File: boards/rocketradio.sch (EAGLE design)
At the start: 29 parts, among them K1 G5LE, T1 2N2222, X1 BU-SMA-H

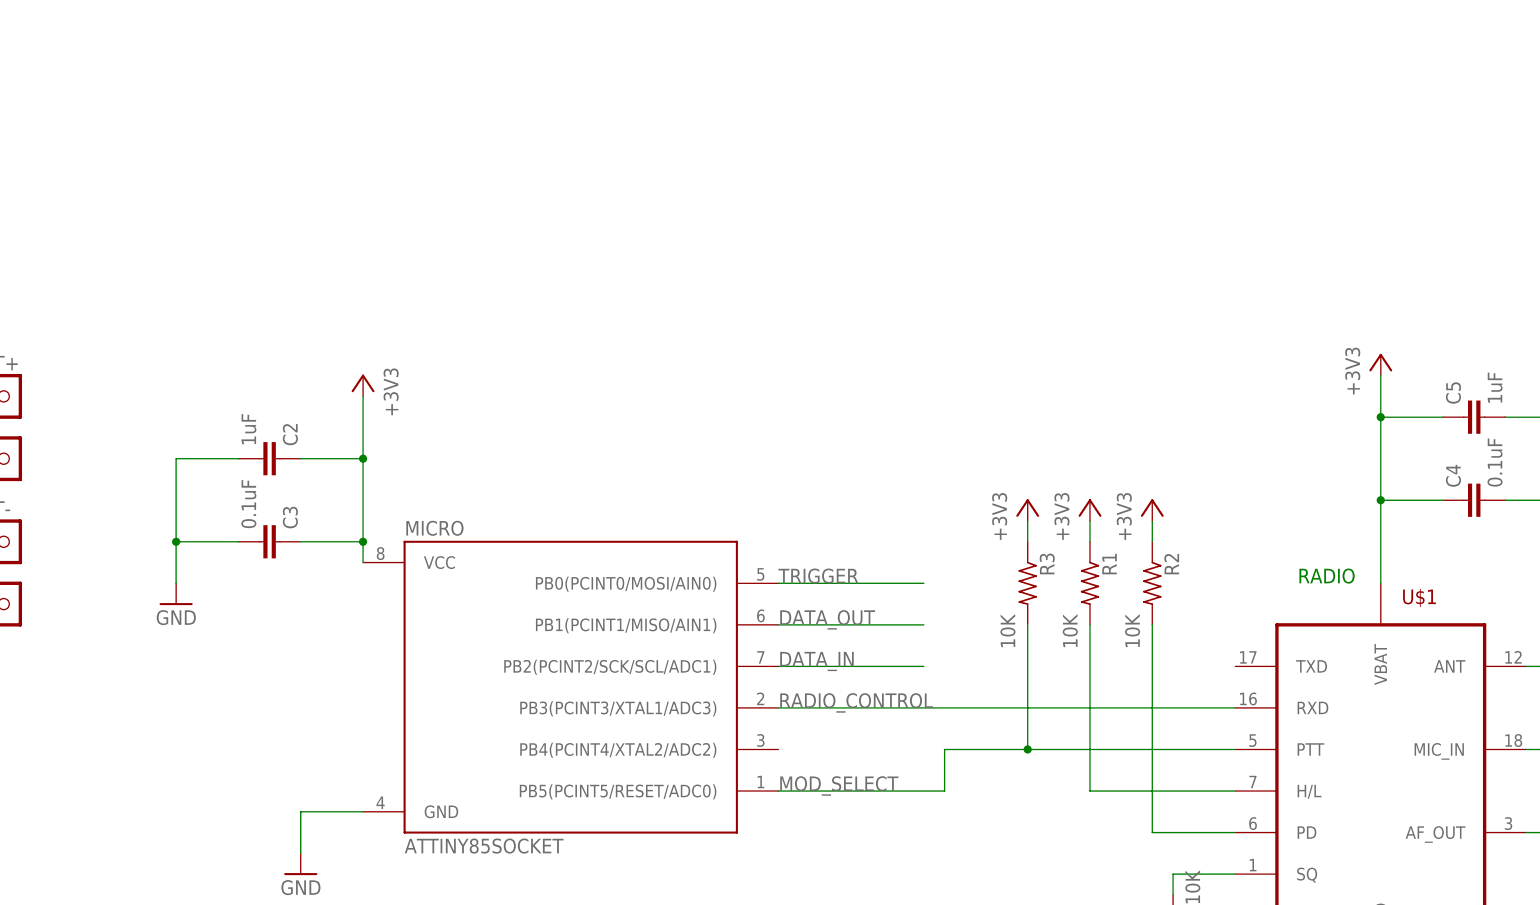
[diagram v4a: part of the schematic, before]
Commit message: use attiny84
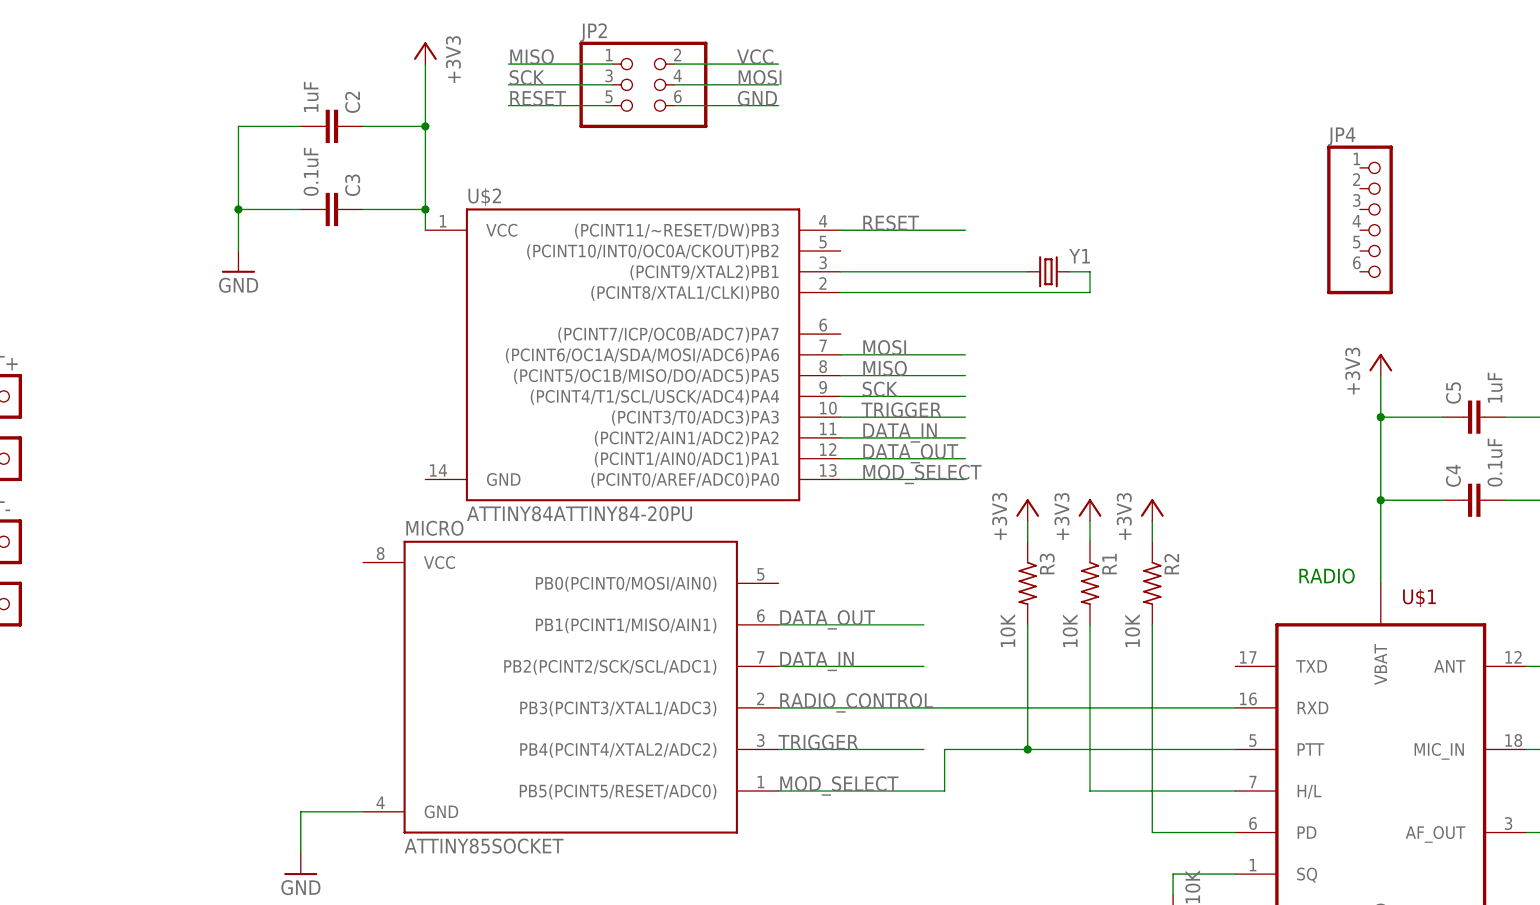
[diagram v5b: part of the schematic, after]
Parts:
- added JP2: (no value), pinhead:PINHD-2X3
- added JP4: (no value), pinhead:PINHD-1X6
- added U$2: ATTINY84ATTINY84-20PU, evan:ATTINY84ATTINY84-20PU
- added Y1: (no value), evan:CRYSTAL
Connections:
- new net MISO: JP2.1, U$2.(PCINT5/OC1B/MISO/DO/ADC5)PA5
- new net MOSI: JP2.4, U$2.(PCINT6/OC1A/SDA/MOSI/ADC6)PA6
- new net N$12: U$2.(PCINT8/XTAL1/CLKI)PB0, Y1.2
- new net N$8: U$2.(PCINT9/XTAL2)PB1, Y1.1
- new net RESET: JP2.5, U$2.(PCINT11/~RESET/DW)PB3
- new net SCK: JP2.3, U$2.(PCINT4/T1/SCL/USCK/ADC4)PA4
- new net VCC: JP2.2
- net +3V3: now also U$2.VCC; no longer MICRO.VCC
- net DATA_IN: now also U$2.(PCINT2/AIN1/ADC2)PA2
- net DATA_OUT: now also U$2.(PCINT1/AIN0/ADC1)PA1
- net GND: now also JP2.6
- net MOD_SELECT: now also U$2.(PCINT0/AREF/ADC0)PA0
- net TRIGGER: now also MICRO.PB4(PCINT4/XTAL2/ADC2), U$2.(PCINT3/T0/ADC3)PA3; no longer MICRO.PB0(PCINT0/MOSI/AIN0)
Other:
- moved on the sheet: C2, C3
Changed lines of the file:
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@@
 <part name="NC" library="evan" deviceset="PINHD-1X1" device=""/>
 <part name="NO" library="evan" deviceset="PINHD-1X1" device=""/>
+<part name="U$2" library="evan" deviceset="ATTINY84" device="ATTINY84-20PU"/>
+<part name="JP2" library="pinhead" deviceset="PINHD-2X3" device=""/>
+<part name="Y1" library="evan" deviceset="CRYSTAL" device=""/>
+<part name="JP4" library="pinhead" deviceset="PINHD-1X6" device=""/>
 </parts>
 <sheets>
@@
 <instance part="GND6" gate="1" x="-144.78" y="25.4" rot="MR0"/>
 <instance part="MICRO" gate="G$1" x="-96.52" y="88.9"/>
-<instance part="+3V4" gate="G$1" x="-121.92" y="127" rot="MR0"/>
-<instance part="C2" gate="G$1" x="-132.08" y="116.84" rot="MR90"/>
-<instance part="C3" gate="G$1" x="-132.08" y="106.68" rot="MR90"/>
-<instance part="GND8" gate="1" x="-144.78" y="99.06" rot="MR0"/>
+<instance part="+3V4" gate="G$1" x="-114.3" y="167.64" rot="MR0"/>
+<instance part="C2" gate="G$1" x="-124.46" y="157.48" rot="MR90"/>
+<instance part="C3" gate="G$1" x="-124.46" y="147.32" rot="MR90"/>
+<instance part="GND8" gate="1" x="-137.16" y="139.7" rot="MR0"/>
 <instance part="GND9" gate="1" x="-129.54" y="66.04" rot="MR0"/>
 <instance part="GND10" gate="1" x="-129.54" y="-7.62" rot="MR0"/>
@@
 <instance part="NC" gate="G$1" x="88.9" y="33.02"/>
 <instance part="NO" gate="G$1" x="53.34" y="33.02" rot="R180"/>
+<instance part="U$2" gate="G$1" x="-88.9" y="129.54"/>
+<instance part="JP2" gate="A" x="-88.9" y="162.56"/>
+<instance part="Y1" gate="G$1" x="-38.1" y="139.7"/>
+<instance part="JP4" gate="A" x="2.54" y="144.78"/>
 </instances>
 <busses>
@@
 <segment>
 <pinref part="C3" gate="G$1" pin="2"/>
-<wire x1="-137.16" y1="106.68" x2="-144.78" y2="106.68" width="0.1524" layer="91"/>
-<wire x1="-144.78" y1="106.68" x2="-144.78" y2="101.6" width="0.1524" layer="91"/>
+<wire x1="-129.54" y1="147.32" x2="-137.16" y2="147.32" width="0.1524" layer="91"/>
+<wire x1="-137.16" y1="147.32" x2="-137.16" y2="142.24" width="0.1524" layer="91"/>
 <pinref part="C2" gate="G$1" pin="2"/>
-<wire x1="-144.78" y1="106.68" x2="-144.78" y2="116.84" width="0.1524" layer="91"/>
-<wire x1="-144.78" y1="116.84" x2="-137.16" y2="116.84" width="0.1524" layer="91"/>
-<junction x="-144.78" y="106.68"/>
+<wire x1="-137.16" y1="147.32" x2="-137.16" y2="157.48" width="0.1524" layer="91"/>
+<wire x1="-137.16" y1="157.48" x2="-129.54" y2="157.48" width="0.1524" layer="91"/>
+<junction x="-137.16" y="147.32"/>
 <pinref part="GND8" gate="1" pin="GND"/>
 </segment>
@@
 <wire x1="40.64" y1="7.62" x2="40.64" y2="10.16" width="0.1524" layer="91"/>
 </segment>
+<segment>
+<pinref part="JP2" gate="A" pin="6"/>
+<wire x1="-83.82" y1="160.02" x2="-71.12" y2="160.02" width="0.1524" layer="91"/>
+<label x="-76.2" y="160.02" size="1.778" layer="95"/>
+</segment>
 </net>
 <net name="+3V3" class="0">
@@
 <pinref part="+3V4" gate="G$1" pin="+3V3"/>
 <pinref part="C2" gate="G$1" pin="1"/>
-<wire x1="-121.92" y1="106.68" x2="-121.92" y2="116.84" width="0.1524" layer="91"/>
-<wire x1="-121.92" y1="116.84" x2="-121.92" y2="124.46" width="0.1524" layer="91"/>
-<wire x1="-129.54" y1="116.84" x2="-121.92" y2="116.84" width="0.1524" layer="91"/>
-<junction x="-121.92" y="116.84"/>
+<wire x1="-114.3" y1="147.32" x2="-114.3" y2="157.48" width="0.1524" layer="91"/>
+<wire x1="-114.3" y1="157.48" x2="-114.3" y2="165.1" width="0.1524" layer="91"/>
+<wire x1="-121.92" y1="157.48" x2="-114.3" y2="157.48" width="0.1524" layer="91"/>
+<junction x="-114.3" y="157.48"/>
 <pinref part="C3" gate="G$1" pin="1"/>
-<wire x1="-129.54" y1="106.68" x2="-121.92" y2="106.68" width="0.1524" layer="91"/>
-<wire x1="-121.92" y1="106.68" x2="-121.92" y2="104.14" width="0.1524" layer="91"/>
-<junction x="-121.92" y="106.68"/>
-<pinref part="MICRO" gate="G$1" pin="VCC"/>
+<wire x1="-121.92" y1="147.32" x2="-114.3" y2="147.32" width="0.1524" layer="91"/>
+<pinref part="U$2" gate="G$1" pin="VCC"/>
+<wire x1="-114.3" y1="147.32" x2="-114.3" y2="144.78" width="0.1524" layer="91"/>
+<junction x="-114.3" y="147.32"/>
 </segment>
 <segment>
@@
 <label x="-71.12" y="76.2" size="1.778" layer="95"/>
 </segment>
+<segment>
+<pinref part="U$2" gate="G$1" pin="(PCINT0/AREF/ADC0)PA0"/>
+<wire x1="-63.5" y1="114.3" x2="-48.26" y2="114.3" width="0.1524" layer="91"/>
+<label x="-60.96" y="114.3" size="1.778" layer="95"/>
+</segment>
 </net>
 <net name="DATA_IN" class="0">
@@
 <wire x1="-71.12" y1="91.44" x2="-53.34" y2="91.44" width="0.1524" layer="91"/>
 <label x="-71.12" y="91.44" size="1.778" layer="95"/>
+</segment>
+<segment>
+<pinref part="U$2" gate="G$1" pin="(PCINT2/AIN1/ADC2)PA2"/>
+<wire x1="-63.5" y1="119.38" x2="-48.26" y2="119.38" width="0.1524" layer="91"/>
+<label x="-60.96" y="119.38" size="1.778" layer="95"/>
 </segment>
 </net>
@@
 <label x="-71.12" y="96.52" size="1.778" layer="95"/>
 </segment>
+<segment>
+<pinref part="U$2" gate="G$1" pin="(PCINT1/AIN0/ADC1)PA1"/>
+<wire x1="-63.5" y1="116.84" x2="-48.26" y2="116.84" width="0.1524" layer="91"/>
+<label x="-60.96" y="116.84" size="1.778" layer="95"/>
+</segment>
 </net>
 <net name="TRIGGER" class="0">
@@
 </segment>
 <segment>
-<pinref part="MICRO" gate="G$1" pin="PB0(PCINT0/MOSI/AIN0)"/>
-<wire x1="-71.12" y1="101.6" x2="-53.34" y2="101.6" width="0.1524" layer="91"/>
-<label x="-71.12" y="101.6" size="1.778" layer="95"/>
+<pinref part="MICRO" gate="G$1" pin="PB4(PCINT4/XTAL2/ADC2)"/>
+<wire x1="-71.12" y1="81.28" x2="-53.34" y2="81.28" width="0.1524" layer="91"/>
+<label x="-71.12" y="81.28" size="1.778" layer="95"/>
+</segment>
+<segment>
+<pinref part="U$2" gate="G$1" pin="(PCINT3/T0/ADC3)PA3"/>
+<wire x1="-63.5" y1="121.92" x2="-48.26" y2="121.92" width="0.1524" layer="91"/>
+<label x="-60.96" y="121.92" size="1.778" layer="95"/>
 </segment>
 </net>
@@
 </segment>
 </net>
+<net name="VCC" class="0">
+<segment>
+<pinref part="JP2" gate="A" pin="2"/>
+<wire x1="-83.82" y1="165.1" x2="-71.12" y2="165.1" width="0.1524" layer="91"/>
+<label x="-76.2" y="165.1" size="1.778" layer="95"/>
+</segment>
+</net>
+<net name="MOSI" class="0">
+<segment>
+<pinref part="JP2" gate="A" pin="4"/>
+<wire x1="-83.82" y1="162.56" x2="-71.12" y2="162.56" width="0.1524" layer="91"/>
+<label x="-76.2" y="162.56" size="1.778" layer="95"/>
+</segment>
+<segment>
+<pinref part="U$2" gate="G$1" pin="(PCINT6/OC1A/SDA/MOSI/ADC6)PA6"/>
+<wire x1="-63.5" y1="129.54" x2="-48.26" y2="129.54" width="0.1524" layer="91"/>
+<label x="-60.96" y="129.54" size="1.778" layer="95"/>
+</segment>
+</net>
+<net name="RESET" class="0">
+<segment>
+<pinref part="JP2" gate="A" pin="5"/>
+<wire x1="-91.44" y1="160.02" x2="-104.14" y2="160.02" width="0.1524" layer="91"/>
+<label x="-104.14" y="160.02" size="1.778" layer="95"/>
+</segment>
+<segment>
+<pinref part="U$2" gate="G$1" pin="(PCINT11/~RESET/DW)PB3"/>
+<wire x1="-63.5" y1="144.78" x2="-48.26" y2="144.78" width="0.1524" layer="91"/>
+<label x="-60.96" y="144.78" size="1.778" layer="95"/>
+</segment>
+</net>
+<net name="SCK" class="0">
+<segment>
+<pinref part="JP2" gate="A" pin="3"/>
+<wire x1="-91.44" y1="162.56" x2="-104.14" y2="162.56" width="0.1524" layer="91"/>
+<label x="-104.14" y="162.56" size="1.778" layer="95"/>
+</segment>
+<segment>
+<pinref part="U$2" gate="G$1" pin="(PCINT4/T1/SCL/USCK/ADC4)PA4"/>
+<wire x1="-63.5" y1="124.46" x2="-48.26" y2="124.46" width="0.1524" layer="91"/>
+<label x="-60.96" y="124.46" size="1.778" layer="95"/>
+</segment>
+</net>
+<net name="MISO" class="0">
+<segment>
+<pinref part="JP2" gate="A" pin="1"/>
+<wire x1="-91.44" y1="165.1" x2="-104.14" y2="165.1" width="0.1524" layer="91"/>
+<label x="-104.14" y="165.1" size="1.778" layer="95"/>
+</segment>
+<segment>
+<pinref part="U$2" gate="G$1" pin="(PCINT5/OC1B/MISO/DO/ADC5)PA5"/>
+<wire x1="-63.5" y1="127" x2="-48.26" y2="127" width="0.1524" layer="91"/>
+<label x="-60.96" y="127" size="1.778" layer="95"/>
+</segment>
+</net>
+<net name="N$8" class="0">
+<segment>
+<pinref part="U$2" gate="G$1" pin="(PCINT9/XTAL2)PB1"/>
+<wire x1="-63.5" y1="139.7" x2="-40.64" y2="139.7" width="0.1524" layer="91"/>
+<pinref part="Y1" gate="G$1" pin="1"/>
+</segment>
+</net>
+<net name="N$12" class="0">
+<segment>
+<pinref part="U$2" gate="G$1" pin="(PCINT8/XTAL1/CLKI)PB0"/>
+<wire x1="-63.5" y1="137.16" x2="-33.02" y2="137.16" width="0.1524" layer="91"/>
+<wire x1="-33.02" y1="137.16" x2="-33.02" y2="139.7" width="0.1524" layer="91"/>
+<pinref part="Y1" gate="G$1" pin="2"/>
+<wire x1="-33.02" y1="139.7" x2="-35.56" y2="139.7" width="0.1524" layer="91"/>
+</segment>
+</net>

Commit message: update rocketradio board, complete
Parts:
- removed JP1, JP3: (no value), evan:PINHD-1X1
- removed JP4: (no value), pinhead:PINHD-1X6
- removed R4: 10K, rcl:R-US_R0603
- removed U$2: ATTINY84ATTINY84-20PU, evan:ATTINY84ATTINY84-20PU
- added 3V3: (no value), evan:PINHD-1X1
- added ISP: (no value), pinhead:PINHD-2X3
- added REG: AP1117-3.3SOT223, evan:AP1117-3.3SOT223
- JP2: device pinhead:PINHD-2X3 -> pinhead:PINHD-1X4
- MICRO: value ATTINY85SOCKET -> ATTINY84ATTINY84-20PU; device evan:ATTINY85SOCKET -> evan:ATTINY84ATTINY84-20PU
- renumbered K1 to RELAY, U$1 to DORJI, X1 to SMA
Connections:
- removed net MISO: JP2.1, U$2.(PCINT5/OC1B/MISO/DO/ADC5)PA5
- removed net MOSI: JP2.4, U$2.(PCINT6/OC1A/SDA/MOSI/ADC6)PA6
- removed net N$3: DORJI.PD, R2.2
- removed net N$5: DORJI.SQ, R4.2
- removed net SCK: JP2.3, U$2.(PCINT4/T1/SCL/USCK/ADC4)PA4
- new net BATT: BATT+.1, C1.1, REG.VI
- new net PA5: DORJI.PD, ISP.1, JP2.4, MICRO.(PCINT5/OC1B/MISO/DO/ADC5)PA5, R2.2
- new net PA6: ISP.4, JP2.3, MICRO.(PCINT6/OC1A/SDA/MOSI/ADC6)PA6
- new net PA7: JP2.2, MICRO.(PCINT7/ICP/OC0B/ADC7)PA7
- new net PB2: JP2.1, MICRO.(PCINT10/INT0/OC0A/CKOUT)PB2
- net +3V3: now also 3V3.1, MICRO.VCC, REG.VO; no longer BATT+.1, C1.1, JP1.1, R1.1, U$2.VCC
- net DATA_IN: now also MICRO.(PCINT3/T0/ADC3)PA3; no longer MICRO.PB2(PCINT2/SCK/SCL/ADC1), U$2.(PCINT2/AIN1/ADC2)PA2
- net DATA_OUT: now also ISP.3, MICRO.(PCINT4/T1/SCL/USCK/ADC4)PA4; no longer MICRO.PB1(PCINT1/MISO/AIN1), U$2.(PCINT1/AIN0/ADC1)PA1
- net GND: now also ISP.6, R1.1, REG.GND; no longer JP2.6, JP3.1, R4.1
- net MOD_SELECT: now also MICRO.(PCINT2/AIN1/ADC2)PA2; no longer MICRO.PB5(PCINT5/RESET/ADC0), U$2.(PCINT0/AREF/ADC0)PA0
- net N$12: now also MICRO.(PCINT8/XTAL1/CLKI)PB0; no longer U$2.(PCINT8/XTAL1/CLKI)PB0
- net N$8: now also MICRO.(PCINT9/XTAL2)PB1; no longer U$2.(PCINT9/XTAL2)PB1
- net RADIO_CONTROL: now also MICRO.(PCINT1/AIN0/ADC1)PA1; no longer MICRO.PB3(PCINT3/XTAL1/ADC3)
- net RESET: now also ISP.5, MICRO.(PCINT11/~RESET/DW)PB3; no longer JP2.5, U$2.(PCINT11/~RESET/DW)PB3
- net TRIGGER: now also MICRO.(PCINT0/AREF/ADC0)PA0; no longer MICRO.PB4(PCINT4/XTAL2/ADC2), U$2.(PCINT3/T0/ADC3)PA3
- net VCC: now also ISP.2; no longer JP2.2
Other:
- note added: "MISO"
- note added: "MOSI"
- note added: "SCK"
- note added: "SLEEP"
- moved on the sheet: BATT+, BATT-, C1, R1
